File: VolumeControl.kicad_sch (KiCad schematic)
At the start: 38 parts, among them J1 Input R/GND/L, J2 SPI, J3 Screw_Terminal_01x03, J4 5V Supply, J5 Lout, J6 Rout, J7 SubOut, U1 AD5290, U2 AD5290, U3 TL082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

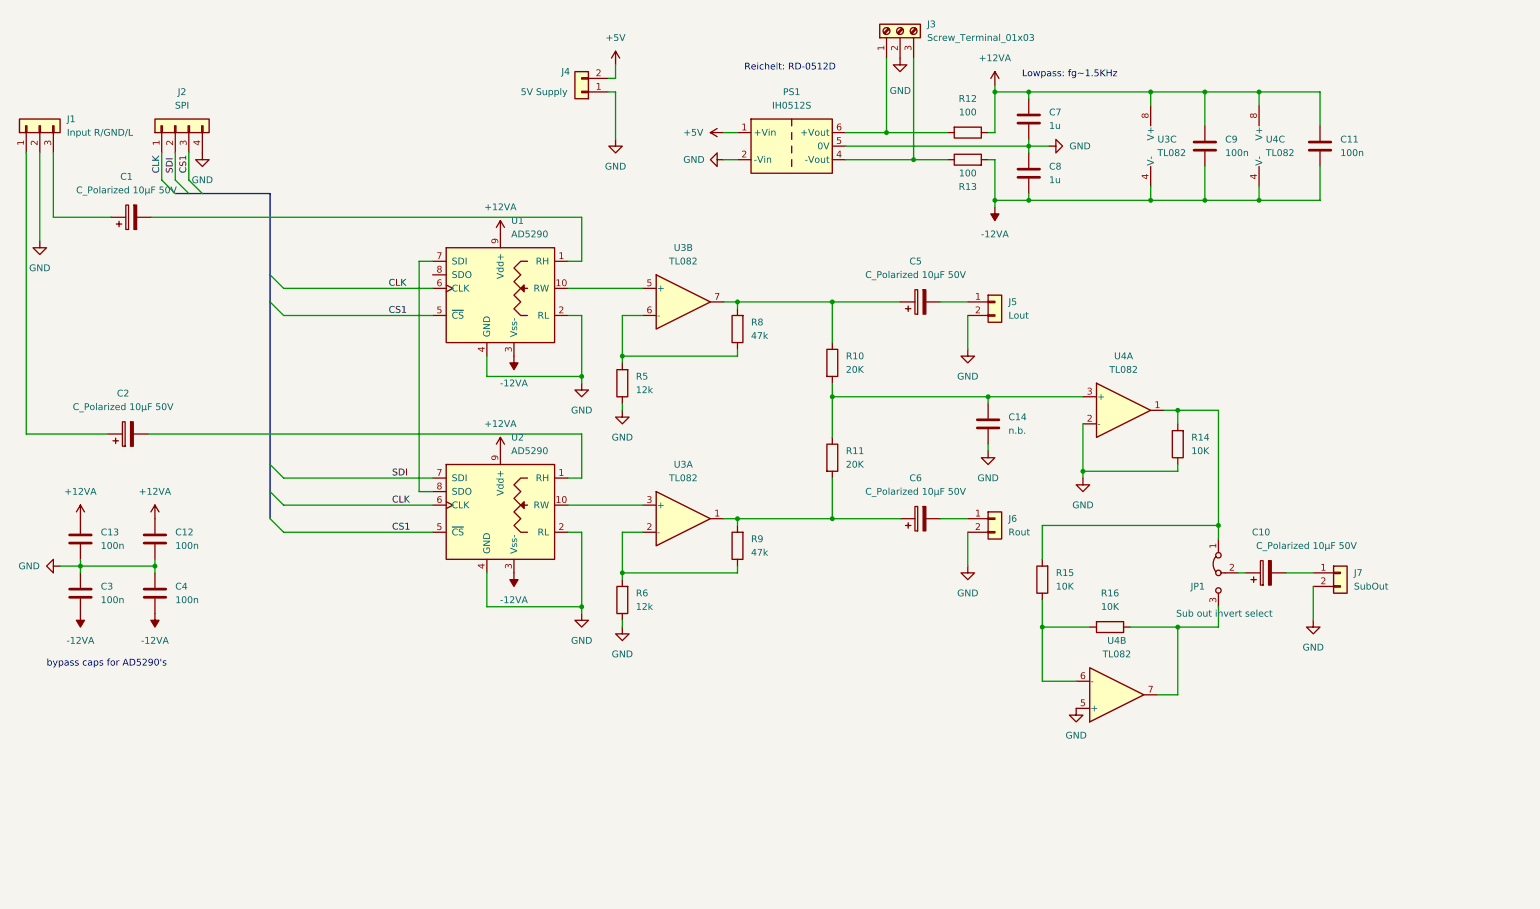
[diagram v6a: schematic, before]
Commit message: added bypass relais
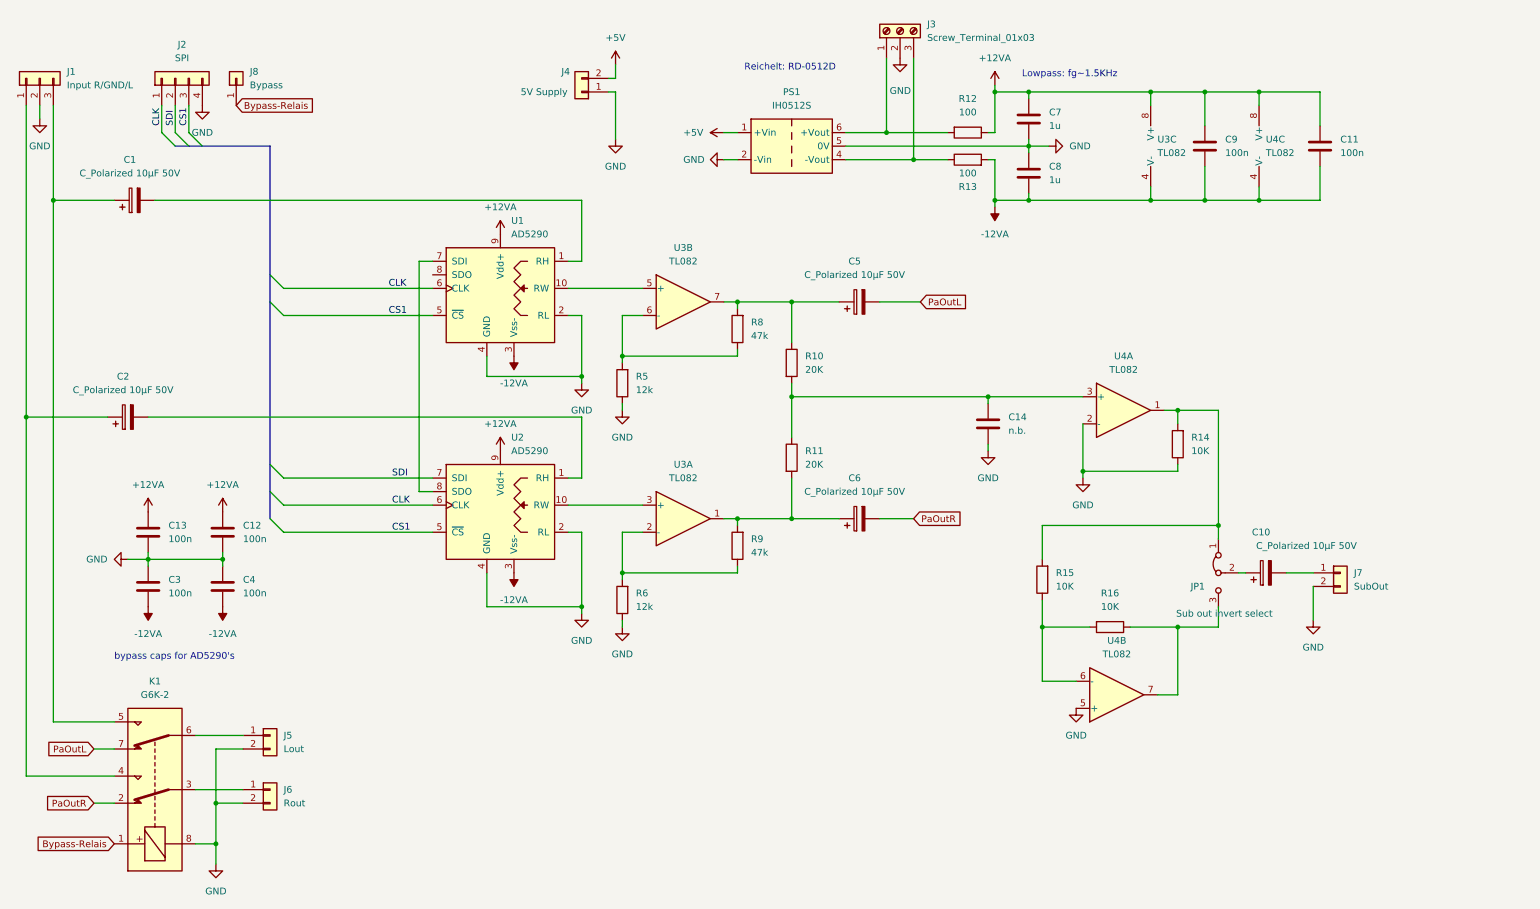
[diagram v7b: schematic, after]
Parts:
- added J8: Bypass, Connector_PinHeader_2.54mm:PinHeader_1x01_P2.54mm_Vertical, symbol Connector_Generic:Conn_01x01
- added K1: G6K-2, Relay_THT:Relay_DPDT_Omron_G6K-2P, symbol Relay:G6K-2
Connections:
- net GND: now also K1.8
- net at C2.1, J1.1 (Pin_1): now also K1.4
- net at J6.1 (Pin_1): now also K1.3; no longer C6.2
- net at C1.1, J1.3 (Pin_3): now also K1.5
- net at J5.1 (Pin_1): now also K1.6; no longer C5.2
- new net Bypass-Relais: J8.1 (Pin_1), K1.1
- new net PaOutL: C5.2, K1.7
- new net PaOutR: C6.2, K1.2
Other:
- moved on the sheet: C1, C12, C13, C2, C3, C4, C5, C6, J1, J2, J5, J6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
